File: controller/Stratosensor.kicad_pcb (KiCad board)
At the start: 2 copper layers, 100 x 100 mm, 40 parts, among them J1 ISP, J10 A45, J11 A67, J2 BME280, J3 BME280, J4 UART, J5 POWER, J6 I2C, J7 I2C, J8 A01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

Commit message: Revision 2 of controller board
Signed-off-by: Alexey Galakhov <agalakhov@gmail.com>
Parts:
- C1, C2: footprint Capacitor_THT:C_Rect_L4.0mm_W2.5mm_P2.50mm -> Capacitor_THT:C_Disc_D4.7mm_W2.5mm_P5.00mm
- moved C2 5.76 mm to (101.0, 123.2), turned to 90 degrees
- moved C1 3.42 mm to (103.5, 124.5), turned to 270 degrees
- moved J3 2.54 mm to (101.6, 63.4)
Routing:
- net /SDA: track 119.3 -> 121.8 mm
- net /SCL: track 126.9 -> 129.4 mm
- net Net-(C2-Pad1): track 11.7 -> 13.6 mm
- net Net-(C1-Pad1): track 11.7 -> 10.3 mm
- removed copper zone on F.Cu, net (none)
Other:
- outline, holes or cut-outs redrawn
- board text added: "AREF"
- board text added: "GND TX RX"
- board text added: "GND VCC"
- board text added: "Gymnasium Brake Project Stratosphere 09-2019"
- board text added: "VCC"
- board text added: "rev. 2"
- board text removed: "Gymnasium Brake Project Stratosphere 08-2019"

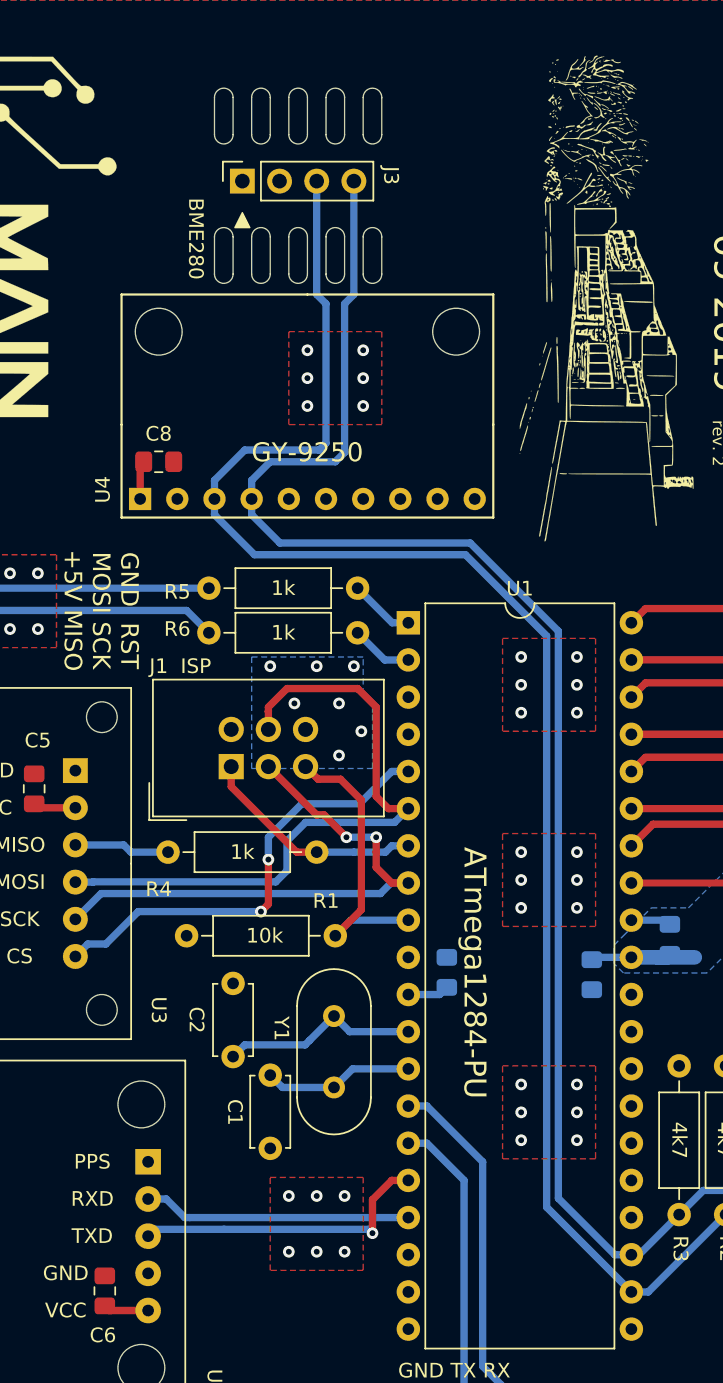
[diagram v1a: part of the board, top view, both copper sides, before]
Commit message: Refined v2 and generated gerbers
Signed-off-by: Alexey Galakhov <agalakhov@snapview.de>
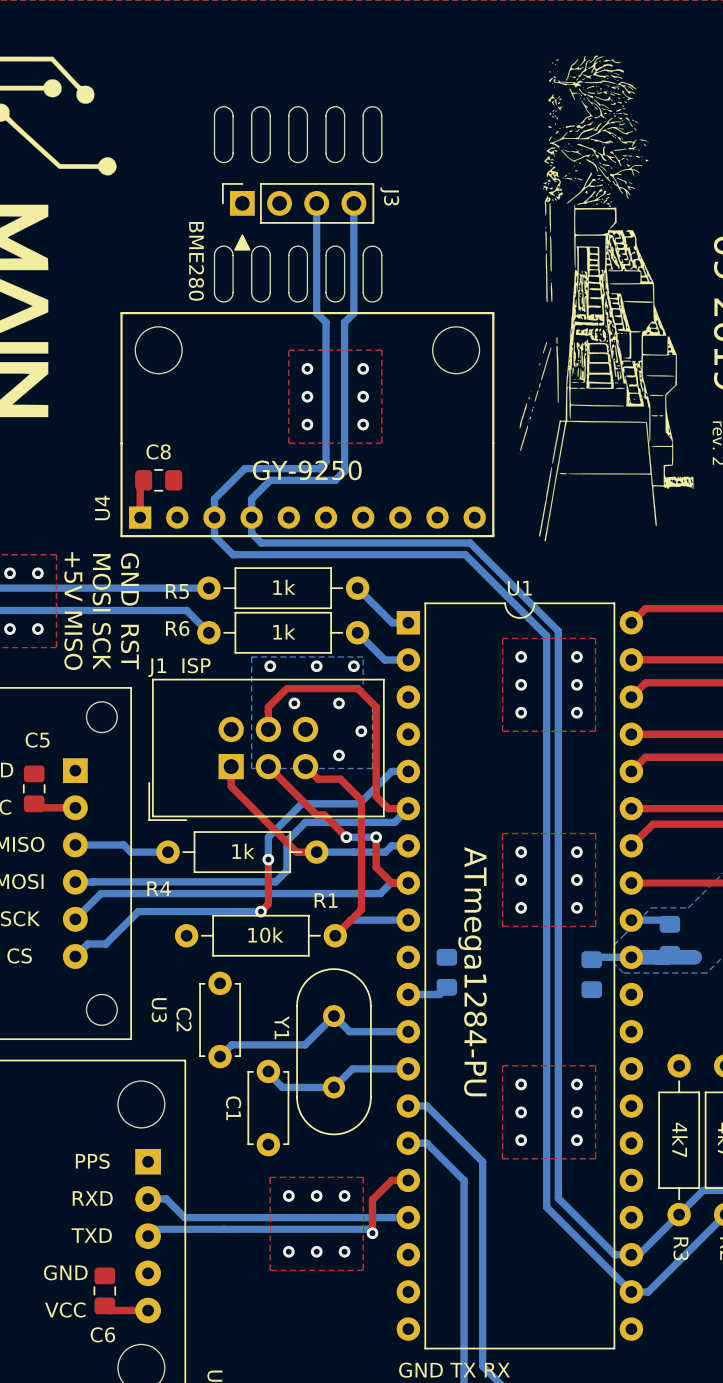
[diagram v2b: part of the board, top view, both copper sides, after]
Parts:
- moved J3 1.52 mm to (101.6, 64.9)
- moved C8 1.27 mm to (95.9, 83.8)
- moved U4 1.27 mm to (106.0, 81.3)
- moved C2 0.89 mm to (100.1, 123.2)
- moved C1 0.28 mm to (103.4, 124.2)
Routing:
- net Net-(C2-Pad1): track 13.6 -> 14.5 mm
- net /SDA: track 121.8 -> 121.3 mm
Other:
- outline, holes or cut-outs redrawn
